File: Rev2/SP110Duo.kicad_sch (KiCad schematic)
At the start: 292 parts, among them J1 USB_C_Receptacle_USB2.0, SW1 RotaryEncoder_Switch, SW10 Switch w/LED, SW100 Switch w/LED, SW101 Switch w/LED, SW102 Switch w/LED, SW103 Switch w/LED, SW104 Switch w/LED, SW105 Switch w/LED, SW106 Switch w/LED, SW107 Switch w/LED, SW108 Switch w/LED, SW109 Switch w/LED, SW11 Switch w/LED, SW110 Switch w/LED, SW12 Switch w/LED, SW13 Switch w/LED, SW14 Switch w/LED, SW15 Switch w/LED, SW16 Switch w/LED, SW17 Switch w/LED, SW18 Switch w/LED, SW19 Switch w/LED, SW2 Switch w/LED, SW20 Switch w/LED, SW21 Switch w/LED, SW22 Switch w/LED, SW23 Switch w/LED, SW24 Switch w/LED, SW25 Switch w/LED, SW26 Switch w/LED, SW27 Switch w/LED, SW28 Switch w/LED, SW29 Switch w/LED, SW3 Switch w/LED, SW30 Switch w/LED, SW31 Switch w/LED, SW32 Switch w/LED, SW33 Switch w/LED, SW34 Switch w/LED, SW35 Switch w/LED, SW36 Switch w/LED, SW37 Switch w/LED, SW38 Switch w/LED, SW39 Switch w/LED, SW4 Switch w/LED, SW40 Switch w/LED, SW41 Switch w/LED, SW42 Switch w/LED, SW43 Switch w/LED, SW44 Switch w/LED, SW45 Switch w/LED, SW46 Switch w/LED, SW47 Switch w/LED, SW48 Switch w/LED, SW49 Switch w/LED, SW5 Switch w/LED, SW50 Switch w/LED, SW51 Switch w/LED, SW52 Switch w/LED, SW53 Switch w/LED, SW54 Switch w/LED, SW55 Switch w/LED, SW56 Switch w/LED, SW57 Switch w/LED, SW58 Switch w/LED, SW59 Switch w/LED, SW6 Switch w/LED, SW60 Switch w/LED, SW61 RotaryEncoder_Switch, SW62 Switch w/LED, SW63 Switch w/LED, SW64 Switch w/LED, SW65 Switch w/LED, SW66 Switch w/LED, SW67 Switch w/LED, SW68 Switch w/LED, SW69 Switch w/LED, SW7 Switch w/LED, SW70 Switch w/LED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

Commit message: schematic layout update
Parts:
- added TP2: 5V, Ghoul:TestPoint, symbol Connector:TestPoint
- renumbered TP2 to TP3, TP3 to TP4, TP4 to TP5, TP5 to TP6, TP6 to TP7
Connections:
- net +5V: now also TP2.1
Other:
- note added: "RESET & BOOT"
- note added: "TEST POINTS"
- moved on the sheet: BOOT1, C10, C13, C14, C22, C23, C24, C3, C4, C5, C6, C7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

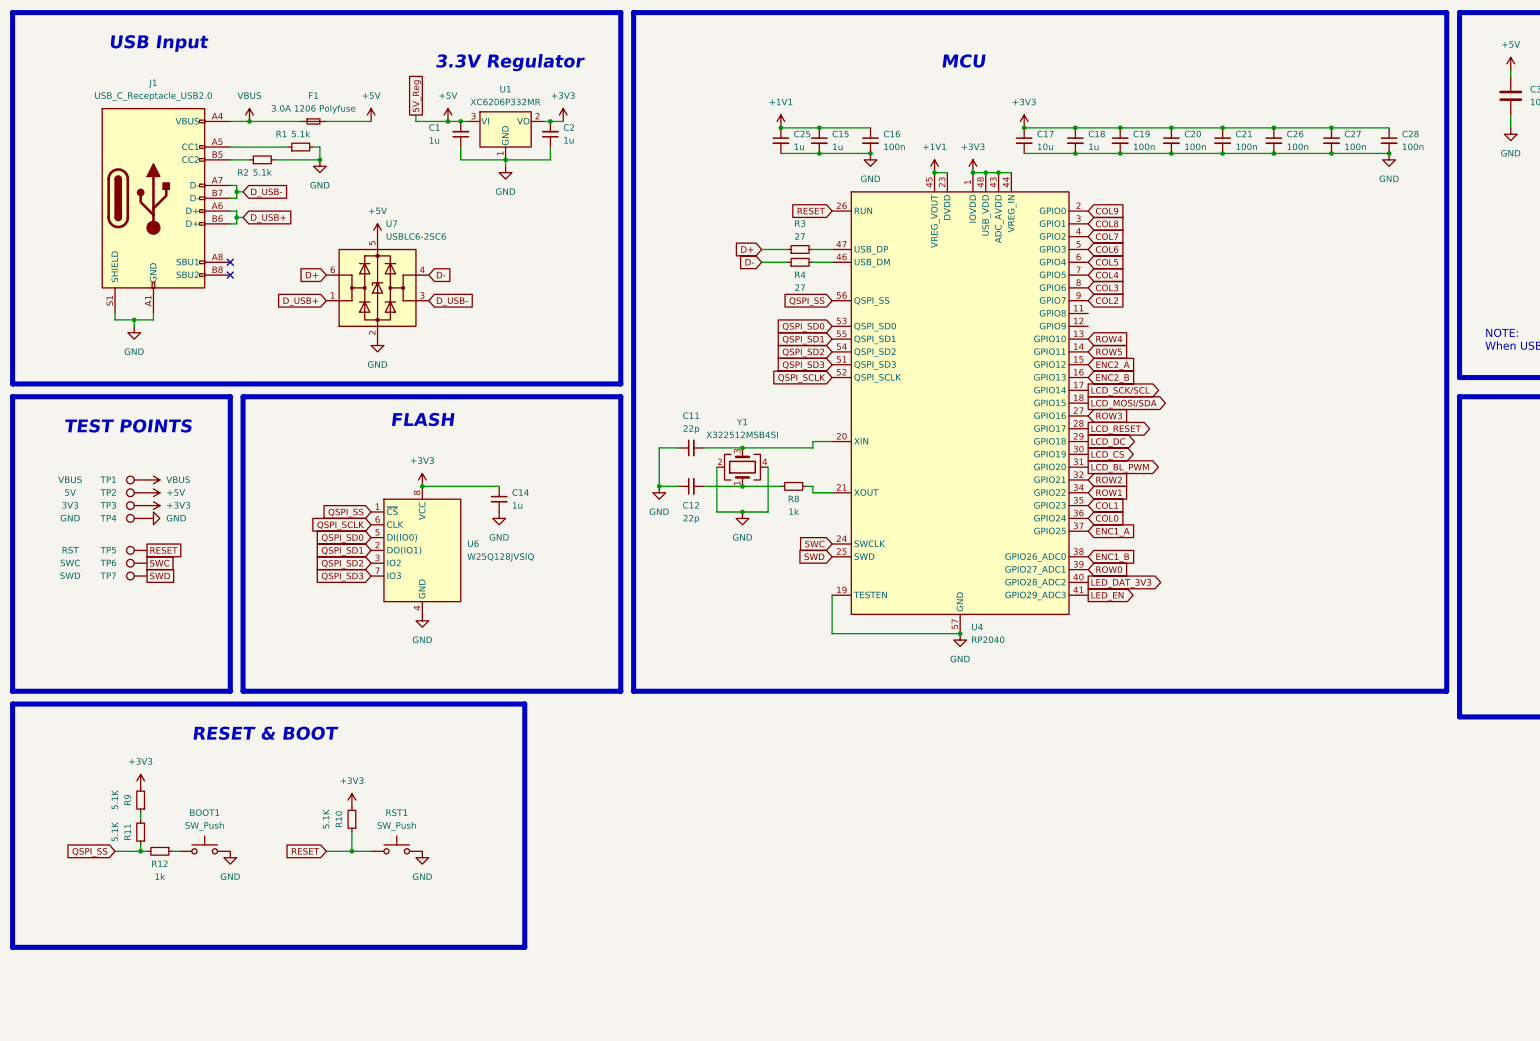
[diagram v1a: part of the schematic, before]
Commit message: update rp2040 version
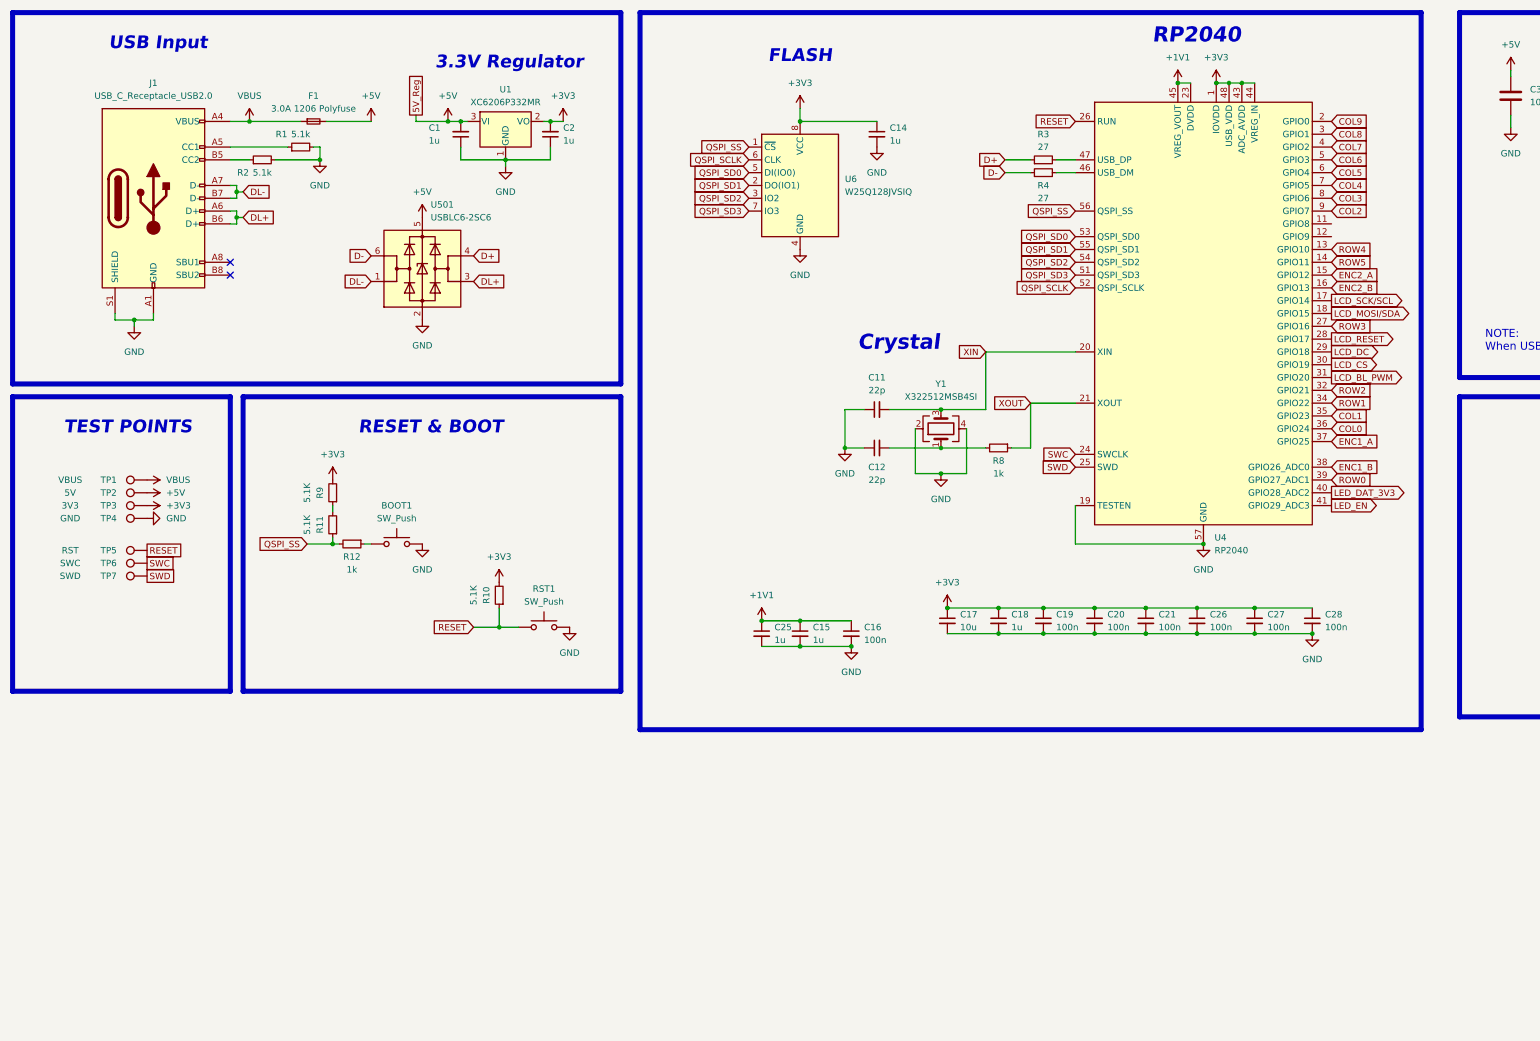
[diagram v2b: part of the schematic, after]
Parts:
- removed U7: USBLC6-2SC6, Package_TO_SOT_SMD:SOT-23-6, symbol Power_Protection:USBLC6-2SC6
- added U501: USBLC6-2SC6, Package_TO_SOT_SMD:SOT-23-6, symbol Power_Protection:USBLC6-2SC6
- J1: footprint PCM_marbastlib-various:USB_C_Receptacle_HRO_TYPE-C-31-M-12 -> reversible-kicad-footprints:HRO-TYPE-C-31-M-12-HandSoldering-NoSBU
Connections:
- net +5V: now also U501.5 (VBUS)
- net D+: now also U501.4 (I/O2)
- net D-: now also U501.6 (I/O1)
- net GND: now also U501.2 (GND)
- net XIN: now reaches C11.2, U4.20 (XIN), Y1.3
- net XOUT: now reaches R8.1, U4.21 (XOUT)
- net D_USB+ renamed DL+
- net DL+: now also U501.3 (I/O2)
- net D_USB- renamed DL-
- net DL-: now also U501.1 (I/O1)
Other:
- note added: "Crystal"
- note added: "RP2040"
- note removed: "MCU"
- moved on the sheet: BOOT1, C11, C12, C14, C15, C16, C17, C18, C19, C20, C21, C25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
